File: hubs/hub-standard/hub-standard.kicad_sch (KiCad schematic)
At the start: 45 parts, among them J1 5VSB_IN, J2 PORT1, J3 PORT2, J4 PORT3, J5 PORT4, J6 USB-C, SW1 SW_RST, SW2 SW_BOOT, U1 ESP32-S3-WROOM-1, U2 TJA1462A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

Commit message: hub-standard: add +5V_HOLD PWR_FLAG (clears ERC error after isolation)
The 5VSB front-end isolation re-topology is wired (manual, GUI): D1 (SS14)
isolation diode with anode on +5VSB and cathode on +5V_HOLD; C1 hold-up
and U3 (LP5907) VIN re-pointed onto +5V_HOLD; R12/R13 (47k/27k) sense
divider on +5VSB -> BLACKOUT_SENSE -> GPIO8 (U1 pin 12). Netlist-verified:
+5VSB and +5V_HOLD are properly split.

+5V_HOLD is fed by a diode (no power-output pin), so it needed a PWR_FLAG
to satisfy ERC - added on-grid. ERC now 0 errors.

Still to place: C_bulk 470uF/10V (LCSC C116423, CP_Elec_6.3x7.7) on
+5VSB. Use the C_Small symbol (CP_Small is absent from the pinned libs;
C1 uses C_Small too) - the footprint carries polarity.

https://claude.ai/code/session_01JVK4H2BFfihS7YDieYFgcV
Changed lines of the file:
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@@
 		)
+	)
+	(symbol
+		(lib_id "cec-power:PWR_FLAG")
+		(at 619.76 99.06 0)
+		(unit 1)
+		(body_style 1)
+		(exclude_from_sim no)(in_bom yes)(on_board yes)(in_pos_files yes)(dnp no)
+		(property "Reference" "#FLG202" (at 619.76 96.52 0) (hide yes)(show_name no)(do_not_autoplace no)(effects (font (size 1.27 1.27))))
+		(property "Value" "PWR_FLAG" (at 619.76 102.87 0) (show_name no)(do_not_autoplace no)(effects (font (size 1.27 1.27))))
+		(property "Footprint" "" (at 619.76 99.06 0) (show_name no)(do_not_autoplace no)(effects (font (size 1.27 1.27))))
+		(property "Datasheet" "" (at 619.76 99.06 0) (show_name no)(do_not_autoplace no)(effects (font (size 1.27 1.27))))
+		(property "Description" "" (at 619.76 99.06 0) (show_name no)(do_not_autoplace no)(effects (font (size 1.27 1.27))))
+		(pin "1")
+		(instances (project "hub-standard" (path "/aa22b2b4-0e2b-481a-a188-ee3f43fcbaa8" (reference "#FLG202") (unit 1))))
+	)
+	(label "+5V_HOLD"
+		(at 619.76 99.06 0)
+		(effects (font (size 1.27 1.27)) (justify left bottom))
 	)
 	(sheet_instances

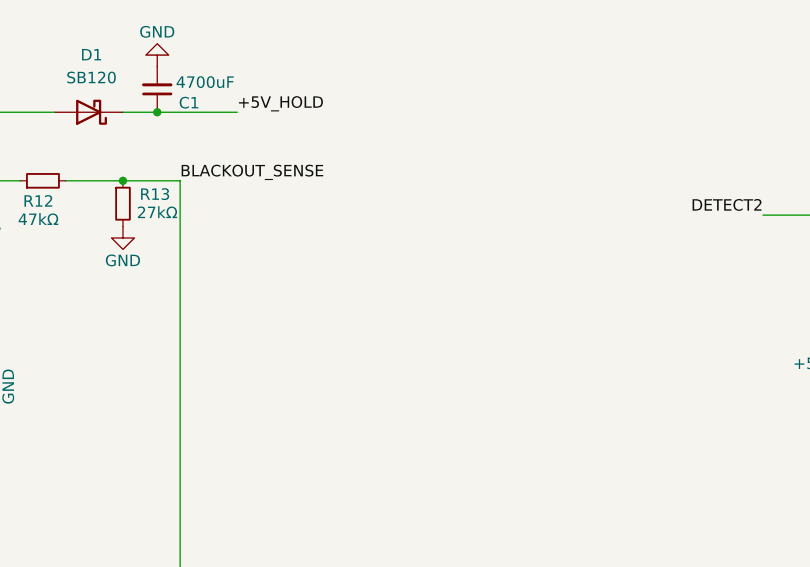
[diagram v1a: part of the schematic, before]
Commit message: hub-standard: place C_bulk 470uF surge cap on +5VSB distribution
Adds the bulk surge cap on the Hub's internal +5VSB rail (downstream of
the U5 TPS2121 mux), to absorb downstream-module load steps locally so
they don't ring back up the cable. Connected +5VSB / GND via power
symbols, matching how the rest of the board names these nets.

Uses the cec-vendor:C_Small symbol (CP_Small is absent from the pinned
libs; C1 uses C_Small too) with the cec-Capacitor_SMD:CP_Elec_6.3x7.7
footprint (470uF/10V V-chip). Deliberately sits on +5VSB, NOT on the
isolated +5V_HOLD hold-up node behind D1 - the 4700uF blackout reservoir
stays separate, and the cap does not smooth the PSU's measured 5VSB
(measurement happens upstream at the 24-pin module, ahead of the cable
and the mux FET).

Netlist verified: C_bulk.1=+5VSB, C_bulk.2=GND; +5V_HOLD unchanged
(C1/C2/D1/U3). ERC 0 errors.

https://claude.ai/code/session_01JVK4H2BFfihS7YDieYFgcV
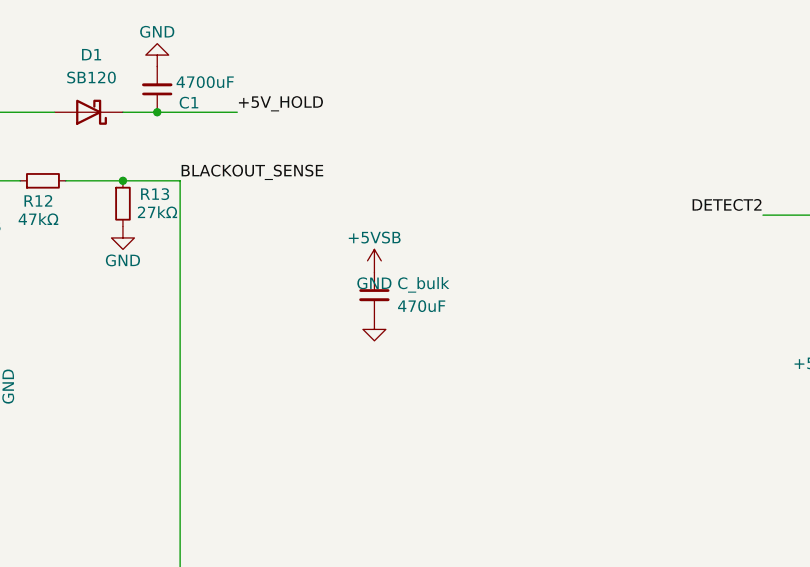
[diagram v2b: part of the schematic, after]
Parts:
- added C_bulk: 470uF, cec-Capacitor_SMD:CP_Elec_6.3x7.7, symbol cec-vendor:C_Small
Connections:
- net +5VSB: now also C_bulk.1
- net GND: now also C_bulk.2
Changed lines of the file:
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@@
 		(effects (font (size 1.27 1.27)) (justify left bottom))
+	)
+	(symbol
+		(lib_id "cec-vendor:C_Small")
+		(at 480.06 113.03 0)
+		(unit 1)
+		(body_style 1)
+		(exclude_from_sim no)
+		(in_bom yes)
+		(on_board yes)
+		(in_pos_files yes)
+		(dnp no)
+		(property "Reference" "C_bulk"
+			(at 482.6 111.76 0)
+			(show_name no)
+			(do_not_autoplace no)
+			(effects
+				(font
+					(size 1.27 1.27)
+				)
+				(justify left)
+			)
+		)
+		(property "Value" "470uF"
+			(at 482.6 114.3 0)
+			(show_name no)
+			(do_not_autoplace no)
+			(effects
+				(font
+					(size 1.27 1.27)
+				)
+				(justify left)
+			)
+		)
+		(property "Footprint" "cec-Capacitor_SMD:CP_Elec_6.3x7.7"
+			(at 480.06 113.03 0)
+			(hide yes)
+			(show_name no)
+			(do_not_autoplace no)
+			(effects
+				(font
+					(size 1.27 1.27)
+				)
+			)
+		)
+		(property "Datasheet" ""
+			(at 480.06 113.03 0)
+			(hide yes)
+			(show_name no)
+			(do_not_autoplace no)
+			(effects
+				(font
+					(size 1.27 1.27)
+				)
+			)
+		)
+		(property "Description" "Bulk surge cap on Hub +5VSB distribution"
+			(at 480.06 113.03 0)
+			(hide yes)
+			(show_name no)
+			(do_not_autoplace no)
+			(effects
+				(font
+					(size 1.27 1.27)
+				)
+			)
+		)
+		(pin "1"
+		)
+		(pin "2"
+		)
+		(instances
+			(project "hub-standard"
+				(path "/aa22b2b4-0e2b-481a-a188-ee3f43fcbaa8"
+					(reference "C_bulk")
+					(unit 1)
+				)
+			)
+		)
+	)
+	(symbol
+		(lib_id "cec-power:+5VSB")
+		(at 480.06 110.49 0)
+		(unit 1)
+		(body_style 1)
+		(exclude_from_sim no)
+		(in_bom yes)
+		(on_board yes)
+		(in_pos_files yes)
+		(dnp no)
+		(property "Reference" "#PWR0201"
+			(at 480.06 113.03 0)
+			(hide yes)
+			(show_name no)
+			(do_not_autoplace no)
+			(effects
+				(font
+					(size 1.27 1.27)
+				)
+			)
+		)
+		(property "Value" "+5VSB"
+			(at 480.06 106.68 0)
+			(show_name no)
+			(do_not_autoplace no)
+			(effects
+				(font
+					(size 1.27 1.27)
+				)
+			)
+		)
+		(property "Footprint" ""
+			(at 480.06 110.49 0)
+			(show_name no)
+			(do_not_autoplace no)
+			(effects
+				(font
+					(size 1.27 1.27)
+				)
+			)
+		)
+		(property "Datasheet" ""
+			(at 480.06 110.49 0)
+			(show_name no)
+			(do_not_autoplace no)
+			(effects
+				(font
+					(size 1.27 1.27)
+				)
+			)
+		)
+		(property "Description" ""
+			(at 480.06 110.49 0)
+			(show_name no)
+			(do_not_autoplace no)
+			(effects
+				(font
+					(size 1.27 1.27)
+				)
+			)
+		)
+		(pin "1"
+		)
+		(instances
+			(project "hub-standard"
+				(path "/aa22b2b4-0e2b-481a-a188-ee3f43fcbaa8"
+					(reference "#PWR0201")
+					(unit 1)
+				)
+			)
+		)
+	)
+	(symbol
+		(lib_id "cec-power:GND")
+		(at 480.06 115.57 0)
+		(unit 1)
+		(body_style 1)
+		(exclude_from_sim no)
+		(in_bom yes)
+		(on_board yes)
+		(in_pos_files yes)
+		(dnp no)
+		(property "Reference" "#PWR0202"
+			(at 480.06 118.11 0)
+			(hide yes)
+			(show_name no)
+			(do_not_autoplace no)
+			(effects
+				(font
+					(size 1.27 1.27)
+				)
+			)
+		)
+		(property "Value" "GND"
+			(at 480.06 111.76 0)
+			(show_name no)
+			(do_not_autoplace no)
+			(effects
+				(font
+					(size 1.27 1.27)
+				)
+			)
+		)
+		(property "Footprint" ""
+			(at 480.06 115.57 0)
+			(show_name no)
+			(do_not_autoplace no)
+			(effects
+				(font
+					(size 1.27 1.27)
+				)
+			)
+		)
+		(property "Datasheet" ""
+			(at 480.06 115.57 0)
+			(show_name no)
+			(do_not_autoplace no)
+			(effects
+				(font
+					(size 1.27 1.27)
+				)
+			)
+		)
+		(property "Description" ""
+			(at 480.06 115.57 0)
+			(show_name no)
+			(do_not_autoplace no)
+			(effects
+				(font
+					(size 1.27 1.27)
+				)
+			)
+		)
+		(pin "1"
+		)
+		(instances
+			(project "hub-standard"
+				(path "/aa22b2b4-0e2b-481a-a188-ee3f43fcbaa8"
+					(reference "#PWR0202")
+					(unit 1)
+				)
+			)
+		)
 	)
 	(sheet_instances

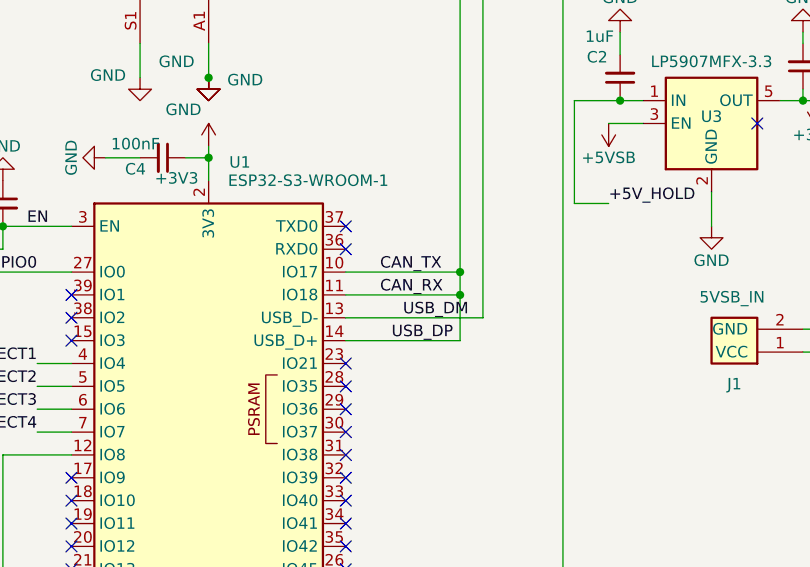
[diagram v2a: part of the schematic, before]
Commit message: hub-standard: fix USB_D+ / CAN short at the ESP32
The IO17/IO18 stubs (CAN_TX/CAN_RX) overshot their labels at x=318.77
and ran to x=327.66, landing on the USB_D+ vertical riser. That T-joined
CAN_TX + CAN_RX + USB_DP into one net, which by name also pulled in the
CAN transceiver TXD/RXD (U2.1/U2.4) and the USB-C D+ pins (J6.A6/B6) -
i.e. USB D+ was shorted to both CAN data lines and two GPIOs.

Trimmed the two stubs back to their CAN_TX/CAN_RX labels (x=318.77) and
removed the two spurious junctions on the riser. Netlist now clean:
  USB_DP = J6.A6/B6 + U1.14
  USB_DM = J6.A7/B7 + U1.13
  CAN_TX = U1.10 + U2.1
  CAN_RX = U1.11 + U2.4
ERC multiple_net_names warning cleared; 0 errors.

https://claude.ai/code/session_01JVK4H2BFfihS7YDieYFgcV
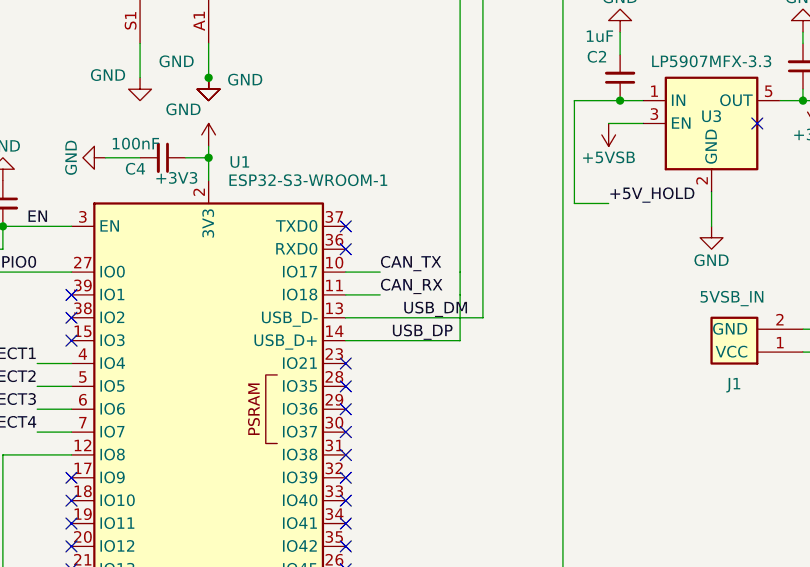
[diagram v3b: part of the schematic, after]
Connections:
- net CAN_RX: no longer J6.A6 (D+), J6.B6 (D+), U1.10 (IO17), U1.14 (USB_D+), U2.1 (TXD)
- new net CAN_TX: U1.10 (IO17), U2.1 (TXD)
- new net USB_DP: J6.A6 (D+), J6.B6 (D+), U1.14 (USB_D+)
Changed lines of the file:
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@@
-	)
-	(junction
-		(at 327.66 86.36)
-		(diameter 0)
-		(color 0 0 0 0)
 	)
 	(junction
@@
 	)
 	(junction
-		(at 327.66 83.82)
-		(diameter 0)
-		(color 0 0 0 0)
-	)
-	(junction
 		(at 537.21 146.05)
 		(diameter 0)
@@
 	(wire
 		(pts
-			(xy 314.96 86.36) (xy 327.66 86.36)
+			(xy 314.96 86.36) (xy 318.77 86.36)
 		)
 		(stroke
@@
 	(wire
 		(pts
-			(xy 314.96 83.82) (xy 327.66 83.82)
-		)
-		(stroke
+			(xy 314.96 83.82) (xy 318.77 83.82)
+		)
+		(stroke

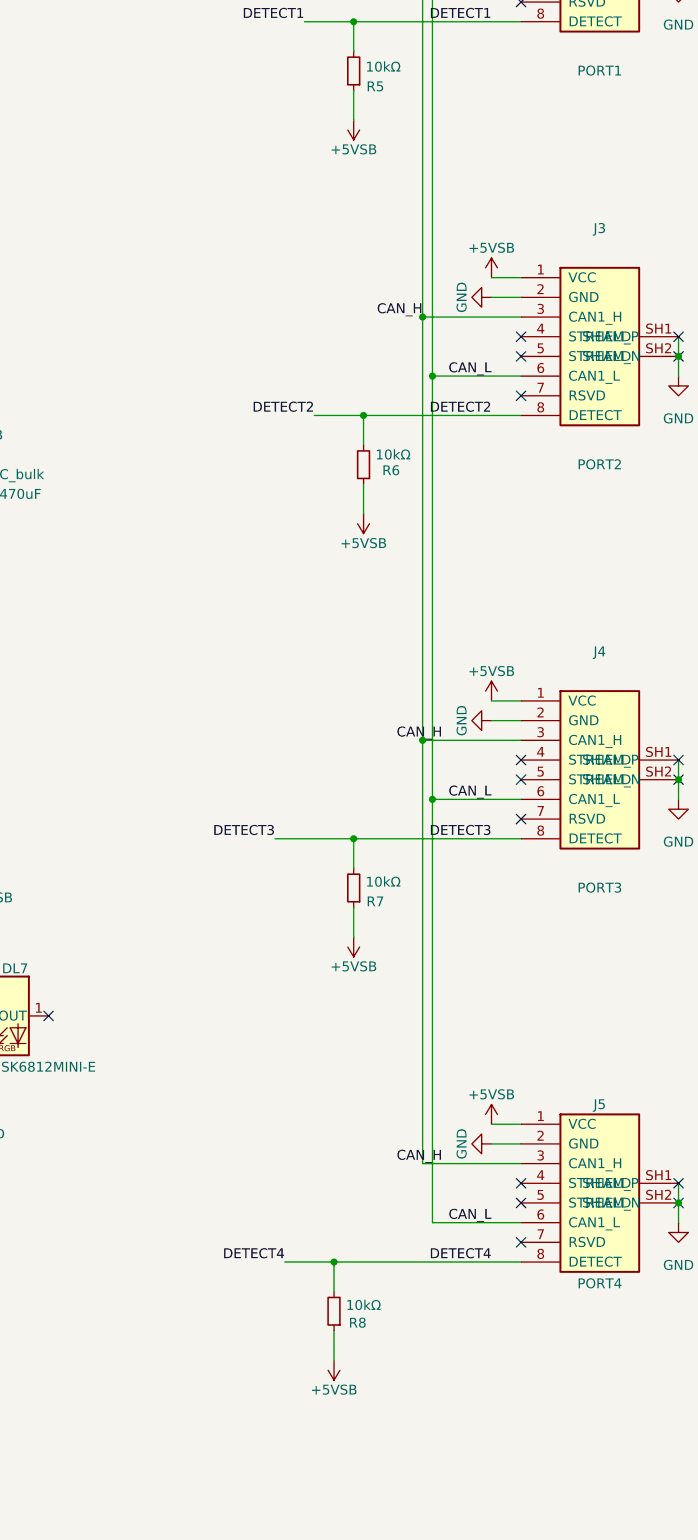
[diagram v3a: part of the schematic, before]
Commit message: hub-standard: fix DETECT pull-up rail + size C1 to its real part
Two pre-layout schematic corrections:

1. DETECT pull-ups (R5-R8, 10k) were pulling up to +5VSB. Spec 2.3
   requires the pull-up to +3V3, NOT 5VSB: the code-table voltages assume
   a 10k/3.3V divider, and a 5V pull-up over-ranges the ESP32 ADC for the
   higher-resistance module codes (22k reserved code -> 3.44V, above the
   3.3V ADC max). Re-pointed the four dedicated pull-up power symbols
   +5VSB -> +3V3. Netlist verified: R5-R8 now on +3V3, +3V3 and +5VSB
   stay separate.

2. C1 hold-up cap footprint was the placeholder CP_Elec_10x10.5 (10mm),
   far too small for a real 4700uF/10V-class part. Swapped to
   CP_Elec_16x17.5 (16mm) to match the sourced part: Panasonic
   EEVFK1C472M (4700uF/16V, FK V-chip, J16 16x16.5mm, LCSC C401967,
   in stock). 16V variant chosen for margin on the ~4.6V +5V_HOLD rail at
   the same footprint. Vendored the 16mm CP_Elec footprint.

ERC 0 errors.

https://claude.ai/code/session_01JVK4H2BFfihS7YDieYFgcV
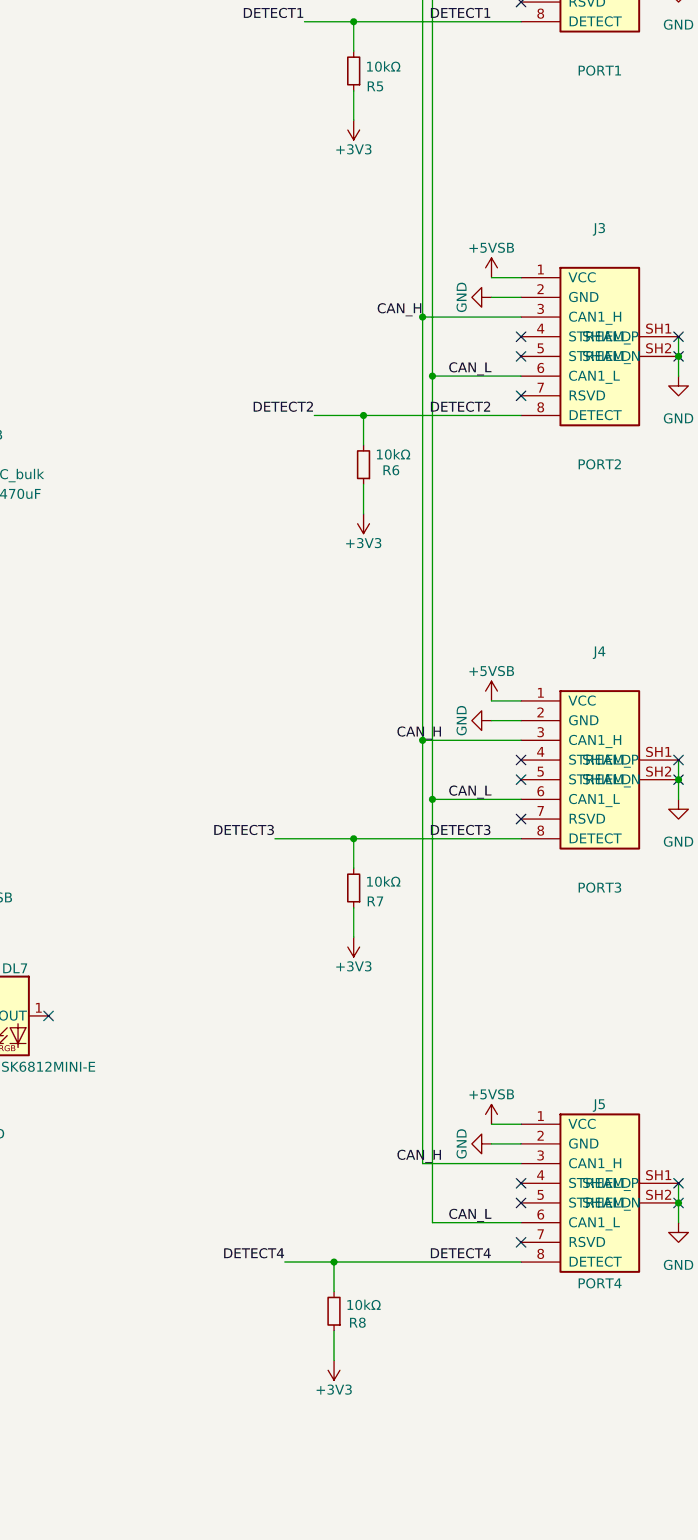
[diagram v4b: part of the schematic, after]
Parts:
- C1: footprint cec-Capacitor_SMD:CP_Elec_10x10.5 -> cec-Capacitor_SMD:CP_Elec_16x17.5
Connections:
- net +3V3: now also R5.1, R6.1, R7.1, R8.1
- net +5VSB: no longer R5.1, R6.1, R7.1, R8.1
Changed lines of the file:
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@@
 	)
 	(symbol
-		(lib_id "cec-power:+5VSB")
+		(lib_id "cec-power:+3V3")
 		(at 528.32 66.04 180)
 		(unit 1)
@@
 			)
 		)
-		(property "Value" "+5VSB"
+		(property "Value" "+3V3"
 			(at 528.32 69.85 0)
 			(show_name no)
@@
 			)
 		)
-		(property "Footprint" "cec-Capacitor_SMD:CP_Elec_10x10.5"
+		(property "Footprint" "cec-Capacitor_SMD:CP_Elec_16x17.5"
 			(at 455.93 90.17 0)
 			(hide yes)
@@
 	)
 	(symbol
-		(lib_id "cec-power:+5VSB")
+		(lib_id "cec-power:+3V3")
 		(at 525.78 226.06 180)
 		(unit 1)
@@
 			)
 		)
-		(property "Value" "+5VSB"
+		(property "Value" "+3V3"
 			(at 525.78 229.87 0)
 			(show_name no)
@@
 	)
 	(symbol
-		(lib_id "cec-power:+5VSB")
+		(lib_id "cec-power:+3V3")
 		(at 529.59 116.84 180)
 		(unit 1)
@@
 			)
 		)
-		(property "Value" "+5VSB"
+		(property "Value" "+3V3"
 			(at 529.59 120.65 0)
 			(show_name no)
@@
 	)
 	(symbol
-		(lib_id "cec-power:+5VSB")
+		(lib_id "cec-power:+3V3")
 		(at 528.32 171.45 180)
 		(unit 1)
@@
 			)
 		)
-		(property "Value" "+5VSB"
+		(property "Value" "+3V3"
 			(at 528.32 175.26 0)
 			(show_name no)
